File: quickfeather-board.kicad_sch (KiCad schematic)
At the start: 101 parts, among them IC1 EOS-S3-QFN, J1 61300211121, J2 PinHeader_1x12_P2.54m_Drill1.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, J3 61301611121, J4 S2B-PH-SM4-TB_LF__SN_, J5 USB-Micro-B_Molex_473460001, J6 PinHeader_2x5_P1.27mm_SMD_Lat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, J7 61300211121, J8 PinHeader_2x8_P2.54mm_Drill1mm, M1 mounting_pad, M2 mounting_pad, M3 mounting_pad, M4 mounting_pad, Q1 NX3008CBKV, Q2 2N7002PV, Q3 2N7002PV, Q4 DMG1012T-7, U1 TPS62821DLCR, U2 MCP73831T-2AC_SOT, U3 GD25Q16CWIGR, U4 DPS310, U5 MC3635, X1 Resonator_12MHz_445

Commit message: [#54927] Standardize EOS 3S
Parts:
- IC1: value EOS-S3-QFN -> EOSAI-S-PUN64; footprint quicklogic-quickfeather-board-footprints:QFN-64_8.5x8.5_EOS -> antmicro-footprints:QFN-64-1EP_8.5x8.5mm_P0.5mm_EP3.3x3.3mm; symbol quickfeather-board:EOS-S3-QFN -> antmicroMicrocontrollers:EOSAI-S-PUN64; Author (none) -> Antmicro; License (none) -> Apache-2.0; MPN EOSA1-S-PUN64 -> EOSAI-S-PUN64
- J1, J7: value 61300211121 -> PinHeader_1x2_P2.54mm_Drill1.1mm; footprint quicklogic-quickfeather-board-footprints:PinHeader_1x2_P2.54_Drill0.9mm -> antmicro-footprints:PinHeader_1x2_P2.54_Drill0.9mm; symbol quickfeather-board:61300211121 -> antmicroGenericPinHeaders:PinHeader_1x2_P2.54mm_Drill1.1mm; Author (none) -> Antmicro; License (none) -> Apache-2.0; Manufacturer Wurth Electronic -> Würth Elektronik
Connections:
- net +3V3: now also IC1.1 (VCCIOA), IC1.12 (VCCIOB), IC1.24 (VCCIOB), IC1.35 (VCCIOB), IC1.46 (AVDD), IC1.50 (LDO_VIN), IC1.52 (LDO_VIN), IC1.58 (VCCIOA), R6.1
- net GND: now also C6.1, C7.2
- net PU_CTRL_USBN: now also R27.1
- net PU_CTRL_USBP: now also R9.1
- net S3IO_8: now also R14.1
- net S3_USB_D_N: now also R7.1
- net S3_USB_D_P: now also R11.1
- net SYS_RST: now also R6.2
- net USB_D_N: now also R27.2, R7.2
- net USB_D_P: now also R11.2, R9.2
- net VDD1: now also IC1.51 (VDD2); no longer IC1.49 (VDD1)
- net VDD2: now also IC1.49 (VDD1); no longer IC1.51 (VDD2)
- net at X1.1: now also C6.2, IC1.44 (XTAL_I)
- net at X1.2: now also C7.1, IC1.45 (XTAL_O)
- net J8.14: no longer names the net of J8.14
- net SWD_SO: no longer names the net of D11.1 (D+)
- no-connect marks 19 -> 21
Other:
- moved on the sheet: C12, C13, C14, C15, C16, C17, C6, C7, J1, J7, R11, R14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

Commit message: [#54927] Add buses
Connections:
- net IMU_INT: no longer IC1.2 (FBIO3/SENSOR_INT_0), R41.6
- net ADC0 renamed ADC.ADC0
- net ADC0_EN renamed ADC.ADC0_{EN}
- net ADC1 renamed ADC.ADC1
- net HEADER_P6 renamed IO.IO43
- net HEADER_RX renamed UART.RX
- net HEADER_TX renamed UART.TX
- net I2C_SCL renamed I2C.SCL
- net I2C_SDA renamed I2C.SDA
- net I2S_CLK renamed I2S.CLK
- net I2S_DOUT renamed I2S.DOUT
- net I2S_WCLK renamed I2S.WCLK
- net PDM_CKO renamed PDM.CKO
- net PDM_DATA renamed PDM.DATA
- net Q_LED_B renamed QLED.B
- net Q_LED_G renamed QLED.G
- net Q_LED_R renamed QLED.R
- net S3IO_10 renamed IO.IO10
- net S3IO_11 renamed IO.IO11
- net S3IO_12 renamed IO.IO12
- net S3IO_13 renamed IO.IO13
- net S3IO_2 renamed IO.IO2
- net S3IO_25 renamed IO.IO25
- net S3IO_30 renamed IO.IO30
- net S3IO_32_I2C1 renamed IO.IO32
- net S3IO_33_I2C1 renamed IO.IO33
- net S3IO_35_SPI_MST_CS3 renamed SPI_HOST.CS3
- net S3IO_4 renamed IO.IO4
- net S3IO_5 renamed IO.IO5
- net S3IO_7 renamed IO.IO7
- net S3IO_8 renamed IO.IO8
- net S3IO_9 renamed IO.IO9
- net SPI_MST_CLK renamed SPI_{HOST}.CLK
- net SPI_MST_CS2 renamed SPI_{HOST}.CS2
- net SPI_MST_MISO renamed SPI_{HOST}.MISO
- net SPI_MST_MOSI renamed SPI_{HOST}.MOSI
- net SPI_MST_SS renamed SPI_{HOST}.CS
- net SPI_SLV_CLK renamed SPI_{DEV}.CLK
- net SPI_SLV_CSn renamed SPI_{DEV}.CS
- net SPI_SLV_MISO renamed SPI_{DEV}.MISO
- net SPI_SLV_MOSI renamed SPI_{DEV}.MOSI
- net SWD_CLK renamed SWD.CLK
- net SWD_IO renamed SWD.IO
- net SYS_RST renamed SWD.SYS_RST
- net USB_D_N renamed USB.D_N
- net USB_D_P renamed USB.D_P
- net USR_BUTTON renamed MISC.USR_BTN
- new net MISC.IMU_INT: IC1.2 (FBIO3/SENSOR_INT_0), R41.6
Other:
- note added: "SPI Debug"
- note removed: "212mA charge current"
- note removed: "IO_19 and IO_20 are bootstrap pins for SPI flash boot. They must be pulled low"
- note removed: "IO_8 and IO_9 are bootstrap pins for HS oscillator. They should be pulled-down for internal HSO"
- note removed: "Maximum power consumption for A and B rails: LDO mode: 65mA (VCCIOA) 114mA (VCCIOB) LDO bypass mode: 77mA (VCCIOA) 269mA (VCCIOB)"
- note removed: "This flash can be replaced with a 64Mbit one (GD25Q64CWIGR)"
- note removed: "operating current for 1V8 supply max. 36mA low-power mode: max. 2.8mA"
- note removed: "operating current max. 20 mA"
- moved on the sheet: C10, C11, C12, C13, C14, C15, C16, C17, C18, C19, C2, C5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

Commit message: [#54927] Update J4
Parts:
- J4: value S2B-PH-SM4-TB_LF__SN_ -> S2B-PH-SM4-TB(LF)(SN); footprint quicklogic-quickfeather-board-footprints:PinHeader_2x1mm_P2mm_SMD_RA -> antmicro-footprints:Conn_JST_PH_1x2_S2B-PH-SM4-TB(LF)(SN); symbol quickfeather-board:S2B-PH-SM4-TB_LF__SN_ -> antmicroWire2BoardConnectors:JST_PH_1x2_S2B-PH-SM4-TB(LF)(SN); Author (none) -> Antmicro; License (none) -> Apache-2.0; Manufacturer JST Sales America Inc. -> JST Automotive Connectors
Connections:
- no-connect marks 21 -> 23
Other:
- moved on the sheet: C10, C9, MIC1, R13, U4

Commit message: [#54927] Minor graphical updates
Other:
- moved on the sheet: C10, C11, C12, C13, C14, C15, C16, C17, C18, C19, C2, C6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

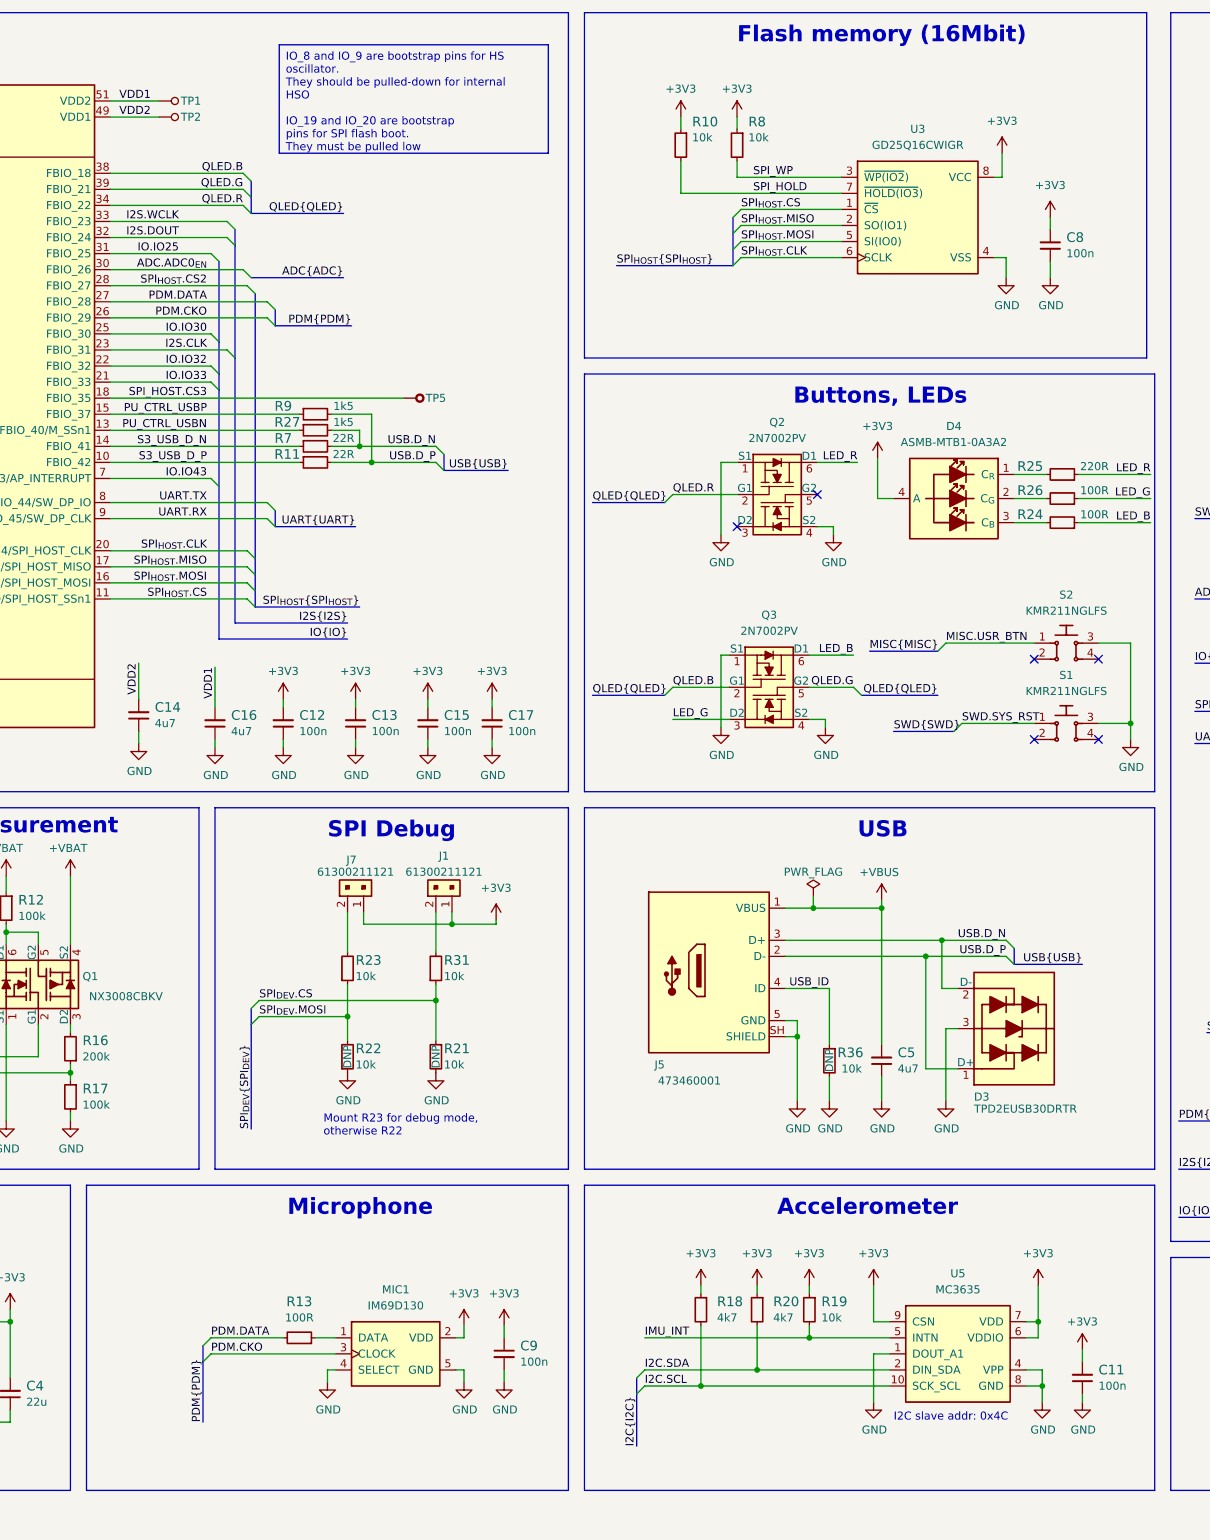
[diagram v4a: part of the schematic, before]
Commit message: [#54927] Update components on PCB to standardized versions
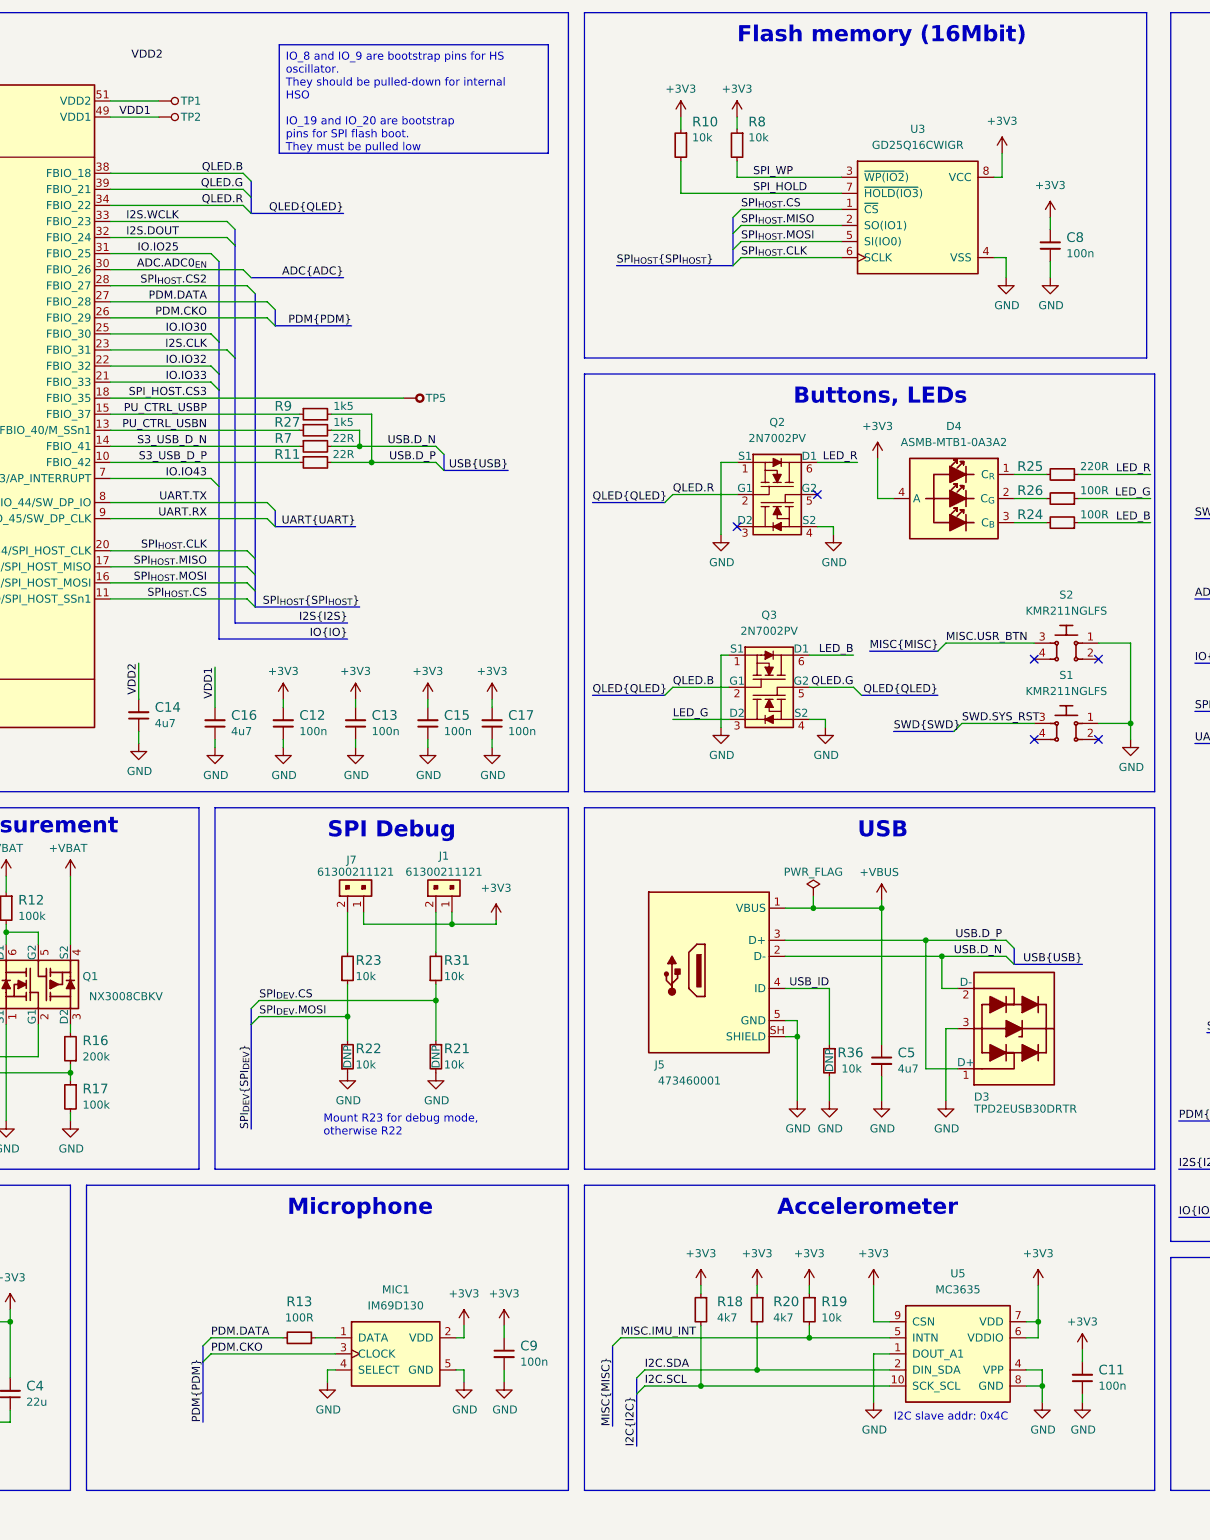
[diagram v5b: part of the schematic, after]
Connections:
- net IMU_INT is gone; now on net MISC.IMU_INT: R19.2, U5.5 (INTN)
- net +VBUS: now also C5.1; no longer C5.2
- net GND: now also C5.2, S1.1, S2.1; no longer C5.1, S1.3, S2.3
- net MISC.USR_BTN: now also S2.3; no longer S2.1
- net SWD.SYS_RST: now also S1.3; no longer S1.1
- net USB.D_N: now also J5.2 (D-); no longer J5.3 (D+)
- net USB.D_P: now also J5.3 (D+); no longer J5.2 (D-)
- net VDD1: now also IC1.49 (VDD1), TP2.1; no longer IC1.51 (VDD2), TP1.1
- net VDD2: no longer IC1.49 (VDD1), TP2.1
- new net: IC1.51 (VDD2), TP1.1
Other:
- moved on the sheet: C5

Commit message: [#54927] Update 2x8 pin header
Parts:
- J8: footprint antmicro-footprints:PinHeadder_MulticompPro_2213S-16G -> antmicro-footprints:PinHeadder_2x8_P2.54mm_Drill1.1mm
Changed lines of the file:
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@@
     (at 167.64 19.05 0) (size 42.545 17.145)
     (stroke (width 0) (type default))
-    (fill (type color) (color 169 171 60 0.3))
+    (fill (type color) (color 171 160 141 0.3))
     (effects (font (size 1.27 1.27)) (justify left top))
   )
@@
       (effects (font (size 1.27 1.27) (thickness 0.15)) (justify left bottom) hide)
     )
-    (property "Footprint" "antmicro-footprints:PinHeadder_MulticompPro_2213S-16G" (at 401.32 150.495 0)
+    (property "Footprint" "antmicro-footprints:PinHeadder_2x8_P2.54mm_Drill1.1mm" (at 401.32 150.495 0)
       (effects (font (size 1.27 1.27) (thickness 0.15)) (justify left bottom) hide)
     )
